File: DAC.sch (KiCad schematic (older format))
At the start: 1 part

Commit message: Add DAC
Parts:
- removed DD?: AD1955, symbol AD1955
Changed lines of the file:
@@
 $Descr A4 11693 8268
 encoding utf-8
-Sheet 1 3
+Sheet 1 1
 Title ""
 Date ""
@@
 Comment4 ""
 $EndDescr
-$Sheet
-S 0    -100 11650 8400
-U 588A0618
-F0 "SatelitesPowerAmplifier" 60
-F1 "SatelitesPowerAmplifier.sch" 60
-$EndSheet
-$Sheet
-S 0    -200 11650 8600
-U 59424E93
-F0 "DAC" 60
-F1 "DAC.sch" 60
-$EndSheet
-$Sheet
-S 0    0    11650 8200
-U 5833169E
-F0 "PowerAmplifier" 60
-F1 "PowerAmplifier.sch" 60
-$EndSheet
-$Comp
-L AD1955 DD?
-U 1 1 5942591C
-P 6700 3350
-F 0 "DD?" H 6700 4297 60  0000 C CNN
-F 1 "AD1955" H 6700 4191 60  0000 C CNN
-F 2 "" H 6700 3600 60  0001 C CNN
-F 3 "" H 6700 3600 60  0001 C CNN
-	1    6700 3350
-	1    0    0    -1
-$EndComp
 $EndSCHEMATC

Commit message: Move DAC circuit from amplifier.sch to DAC.sch
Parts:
- added DD?: AD1955, symbol AD1955
- added DD?: SRC4392I, symbol SRC4392I
- added J?: CONN_01X07, symbol CONN_01X07
- added J?: CONN_01X09, symbol CONN_01X09
- added R?: 3.3k, symbol R
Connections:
- net labels added: GNDA
- wire segments 0 -> 56
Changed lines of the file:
@@
 Comment4 ""
 $EndDescr
+$Comp
+L AD1955 DD?
+U 1 1 5943ADF1
+P 6150 3400
+F 0 "DD?" H 6150 4347 60  0000 C CNN
+F 1 "AD1955" H 6150 4241 60  0000 C CNN
+F 2 "" H 6150 3650 60  0001 C CNN
+F 3 "" H 6150 3650 60  0001 C CNN
+	1    6150 3400
+	1    0    0    -1
+$EndComp
+$Comp
+L SRC4392I DD?
+U 1 1 5943BE8C
+P 3750 2650
+F 0 "DD?" H 3750 4347 60  0000 C CNN
+F 1 "SRC4392I" H 3750 4241 60  0000 C CNN
+F 2 "" H 3800 3350 60  0001 C CNN
+F 3 "" H 3800 3350 60  0001 C CNN
+	1    3750 2650
+	1    0    0    -1
+$EndComp
+Wire Wire Line
+	5500 2900 4400 2900
+Wire Wire Line
+	4400 3000 5300 3000
+Wire Wire Line
+	5300 3000 5300 2700
+Wire Wire Line
+	5300 2700 5500 2700
+Wire Wire Line
+	5500 2800 5200 2800
+Wire Wire Line
+	5200 2800 5200 3100
+Wire Wire Line
+	5200 3100 4400 3100
+Wire Wire Line
+	5500 3700 5400 3700
+Wire Wire Line
+	5400 3700 5400 4250
+Wire Wire Line
+	5400 4250 7200 4250
+Wire Wire Line
+	7200 4250 7200 2300
+Wire Wire Line
+	5500 3600 5300 3600
+Wire Wire Line
+	5300 3600 5300 4350
+Wire Wire Line
+	5300 4350 7300 4350
+Wire Wire Line
+	7300 4350 7300 2400
+Wire Wire Line
+	7200 2300 7700 2300
+Wire Wire Line
+	4400 2000 7700 2000
+Wire Wire Line
+	4400 1900 7700 1900
+Wire Wire Line
+	4400 1800 7700 1800
+Wire Wire Line
+	4400 1700 7700 1700
+Wire Wire Line
+	3100 2600 3000 2600
+Wire Wire Line
+	3000 2600 3000 900
+Wire Wire Line
+	3000 900  7600 900
+Wire Wire Line
+	7600 900  7600 1600
+Wire Wire Line
+	7600 1600 7700 1600
+Wire Wire Line
+	7300 2400 7700 2400
+Wire Wire Line
+	4400 2100 5050 2100
+Wire Wire Line
+	5050 2100 5050 1200
+Wire Wire Line
+	5050 1200 5550 1200
+Wire Wire Line
+	4400 2200 5150 2200
+Wire Wire Line
+	5150 2200 5150 1300
+Wire Wire Line
+	5150 1300 5550 1300
+Wire Wire Line
+	4400 2300 5250 2300
+Wire Wire Line
+	5250 2300 5250 1400
+Wire Wire Line
+	5250 1400 5550 1400
+Wire Wire Line
+	4400 2400 5350 2400
+Wire Wire Line
+	5350 2400 5350 1500
+Wire Wire Line
+	5350 1500 5550 1500
+Wire Wire Line
+	4400 1300 4950 1300
+Wire Wire Line
+	4950 1300 4950 1100
+Wire Wire Line
+	4950 1100 5550 1100
+Wire Wire Line
+	4400 1200 4850 1200
+Wire Wire Line
+	4850 1200 4850 1000
+Wire Wire Line
+	4850 1000 5550 1000
+Wire Wire Line
+	4400 2500 5450 2500
+Wire Wire Line
+	5450 2500 5450 1600
+Wire Wire Line
+	5450 1600 5550 1600
+$Comp
+L CONN_01X07 J?
+U 1 1 5A0C051E
+P 5750 1300
+F 0 "J?" H 5828 1341 50  0000 L CNN
+F 1 "CONN_01X07" H 5828 1250 50  0000 L CNN
+F 2 "" H 5750 1300 50  0001 C CNN
+F 3 "" H 5750 1300 50  0001 C CNN
+	1    5750 1300
+	1    0    0    -1
+$EndComp
+$Comp
+L CONN_01X09 J?
+U 1 1 5A0C063A
+P 7900 2000
+F 0 "J?" H 7978 2041 50  0000 L CNN
+F 1 "CONN_01X09" H 7978 1950 50  0000 L CNN
+F 2 "" H 7900 2000 50  0001 C CNN
+F 3 "" H 7900 2000 50  0001 C CNN
+	1    7900 2000
+	1    0    0    -1
+$EndComp
+$Comp
+L R R?
+U 1 1 5B040832
+P 5200 4500
+F 0 "R?" H 5270 4546 50  0000 L CNN
+F 1 "3.3k" H 5270 4455 50  0000 L CNN
+F 2 "" V 5130 4500 50  0001 C CNN
+F 3 "" H 5200 4500 50  0001 C CNN
+	1    5200 4500
+	1    0    0    -1
+$EndComp
+Wire Wire Line
+	5200 4350 5200 3500
+Wire Wire Line
+	5200 3500 5500 3500
+$Comp
+L GNDA #PWR?
+U 1 1 5B0409AF
+P 5200 4700
+F 0 "#PWR?" H 5200 4450 50  0001 C CNN
+F 1 "GNDA" H 5205 4527 50  0000 C CNN
+F 2 "" H 5200 4700 50  0001 C CNN
+F 3 "" H 5200 4700 50  0001 C CNN
+	1    5200 4700
+	1    0    0    -1
+$EndComp
+Wire Wire Line
+	5200 4700 5200 4650
+Wire Wire Line
+	6800 3400 7100 3400
+Wire Wire Line
+	7100 3400 7100 2200
+Wire Wire Line
+	7100 2200 7700 2200
+Wire Wire Line
+	6800 3300 7000 3300
+Wire Wire Line
+	7000 3300 7000 2100
+Wire Wire Line
+	7000 2100 7700 2100
 $EndSCHEMATC

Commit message: DAC modifications
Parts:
- added J?: I2S 1, symbol CONN_01X05
- added J?: I2S 2, symbol CONN_01X05
- added J?: I2S USB, symbol CONN_01X05
- added J?: I2S HDMI, symbol CONN_01X05
- added J?: Ext DAC, symbol CONN_01X05
- added JP? (x3): DAC ON, symbol Jumper_NC_Small
- added U? (x2): 74HC244, symbol 74HC244
- added U?: ATMEGA88A-PU, DIL28, symbol ATMEGA88A-PU
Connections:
- net labels added: GNDD
- wire segments 56 -> 199
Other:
- moved on the sheet: DD?, R?

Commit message: DAC changes
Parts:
- removed J?: CONN_01X07, symbol CONN_01X07
- removed J?: CONN_01X09, symbol CONN_01X09
- removed J?: I2S 1, symbol CONN_01X05
- removed J?: I2S 2, symbol CONN_01X05
- removed J?: I2S USB, symbol CONN_01X05
- removed J?: I2S HDMI, symbol CONN_01X05
- removed J?: Ext DAC, symbol CONN_01X05
- removed U? (x2): 74HC244, symbol 74HC244
- added C? (x8): 0.1, symbol C_Small
- added DD??: CDCLVC1104, symbol CDCLVC1104
- added J?: To external DAC, symbol CONN_01X04
- added J?: SRC Pins, symbol CONN_01X12
- added J?: DSD Input, symbol CONN_01X04
- added J?: I2S Input, symbol CONN_01X04
- added J?: DAC Pins, symbol CONN_01X05
- added J?: SPDIF Inputs, symbol CONN_01X05
- added J?: CONN_01X05, symbol CONN_01X05
- added R? (x7): 75, symbol R
- added R?: 1k, symbol R
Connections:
- wire segments 199 -> 213
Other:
- moved on the sheet: DD?, JP?, R?, U?

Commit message: Add power
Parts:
- removed R?: 1k, symbol R
- added C? (x2): 2.2, symbol CP_Small
- added C? (x3): 0.1, symbol C_Small
- added C? (x6): 1.0, symbol C_Small
- added C?: 3.3, symbol CP_Small
- added C?: 6.8, symbol CP_Small
- added DA? (x3): LP5900, symbol LP5900
- added J?: MUTE/~RST, symbol CONN_01X03
- added J?: I2S Fs, symbol CONN_01X04
- added R?: 10, symbol R-RESCUE-amplifier
- added R?: 1k, symbol R
- J?: value CONN_01X05 -> Input select
- R? (x8): symbol R -> R-RESCUE-amplifier
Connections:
- net labels added: +1V8, +3.3V, +3V3, +5V, DGND
- wire segments 213 -> 261
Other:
- moved on the sheet: DD??, J?, U?

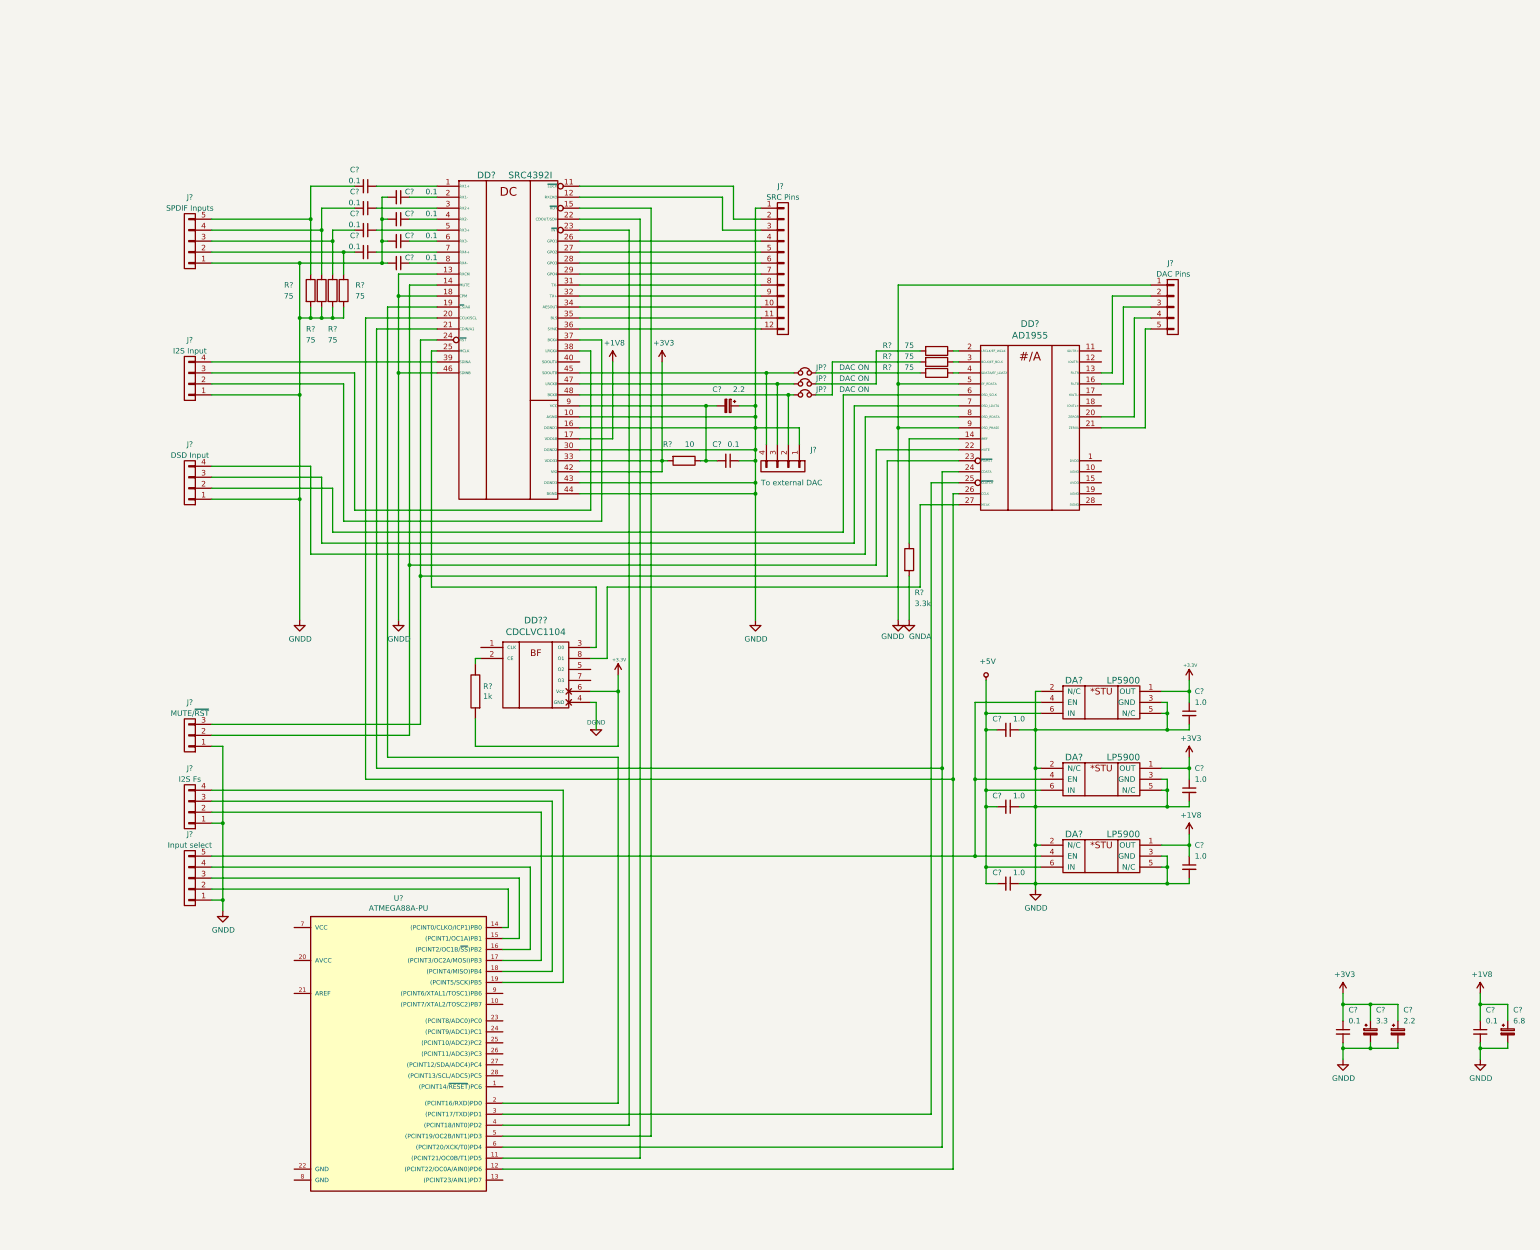
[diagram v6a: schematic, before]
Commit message: Add generators and ad8066
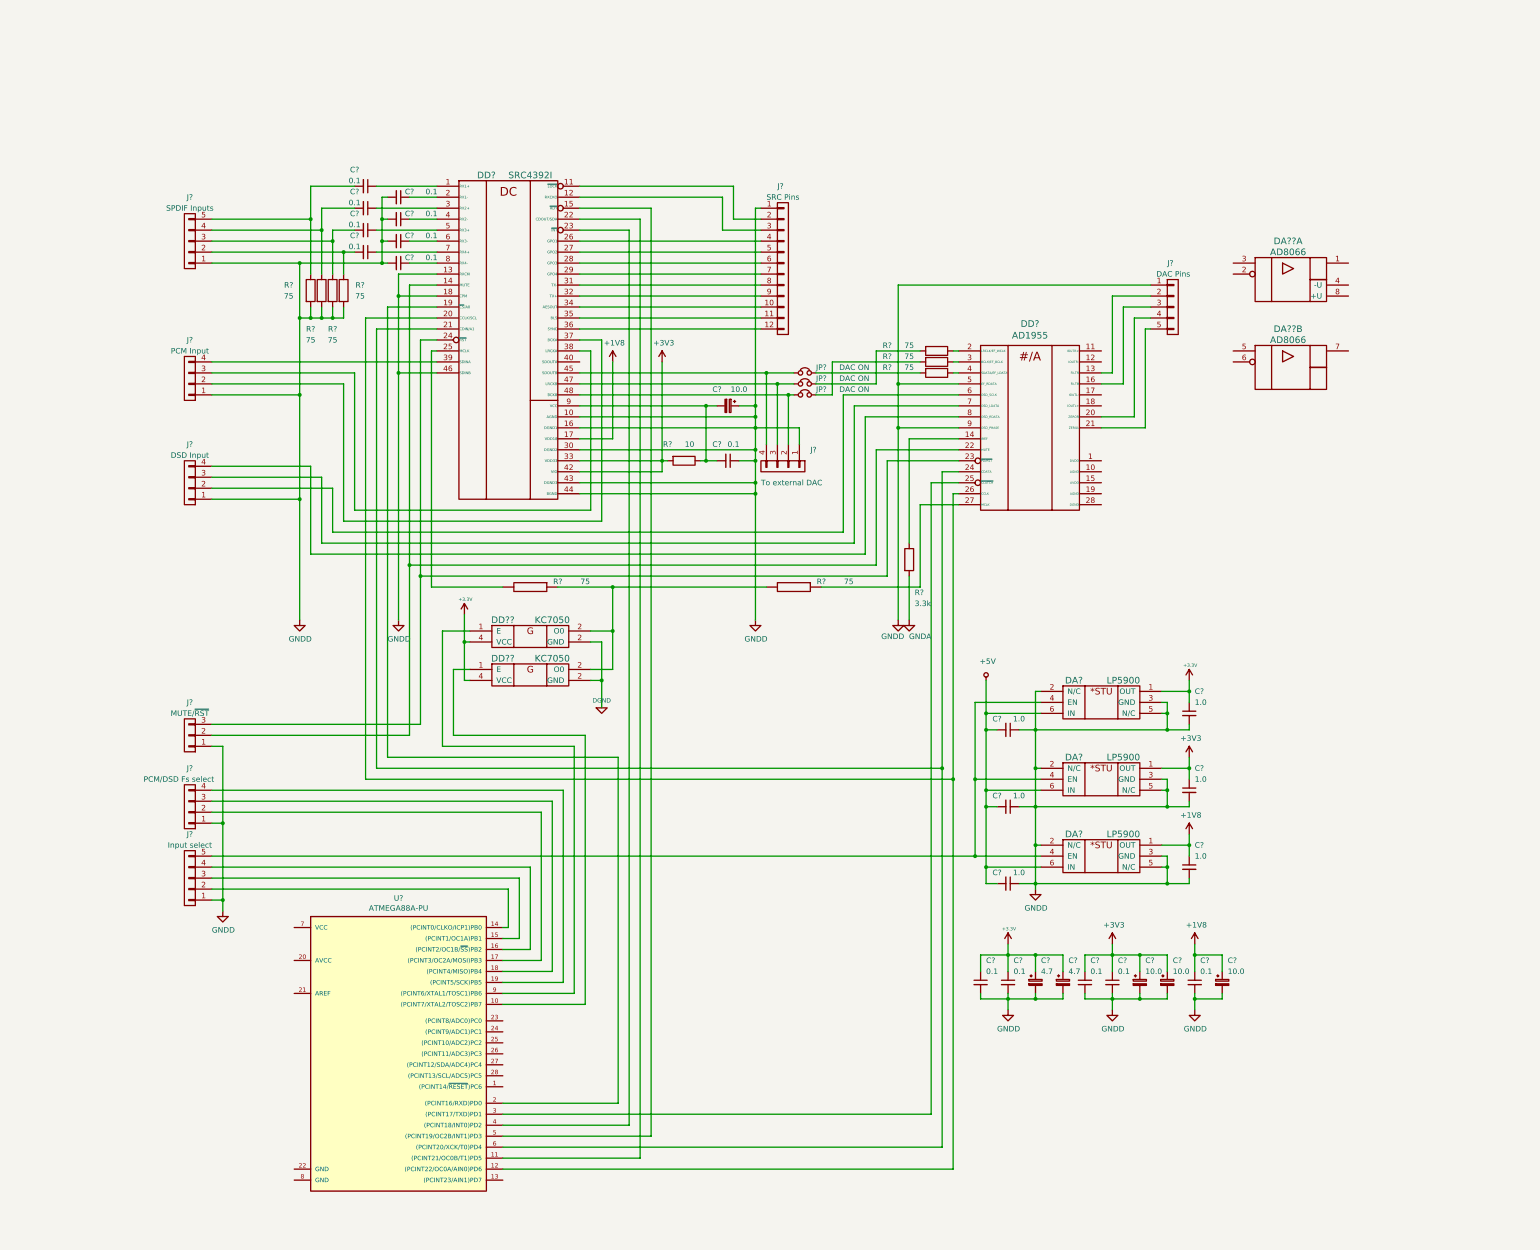
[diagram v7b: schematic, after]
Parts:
- removed DD??: CDCLVC1104, symbol CDCLVC1104
- removed R?: 1k, symbol R
- added C? (x3): 0.1, symbol C_Small
- added C? (x2): 4.7, symbol CP_Small
- added DA?? (x2): AD8066, symbol AD8066
- added DD?? (x2): KC7050, symbol KC7050
- added R? (x2): 75, symbol R
- C? (x2): value 2.2 -> 10.0
- C?: value 3.3 -> 10.0
- C?: value 6.8 -> 10.0
- J?: value I2S Input -> PCM Input
- J?: value I2S Fs -> PCM/DSD Fs select
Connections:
- net +3V3: now also C?.1, C?.1, C?.1, C?.1, C?.1, DD??.4 (VCC), DD??.4 (VCC)
- net DGND: now also DD??.2 (O0), DD??.2 (O0)
- net GNDD: now also C?.2, C?.2, C?.2, C?.2, C?.2
- net at DD?.27 (MCLK): now also R?.1
- net at DD?.25 (MCLK): now also R?.2
- net at U?.10 ((PCINT7/XTAL2/TOSC2)PB7): now also DD??.1 (E)
- net at U?.9 ((PCINT6/XTAL1/TOSC1)PB6): now also DD??.1 (E)
- new net: DD??.2 (O0), DD??.2 (O0), R?.1, R?.2
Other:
- moved on the sheet: C?

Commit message: Add more power for DAC
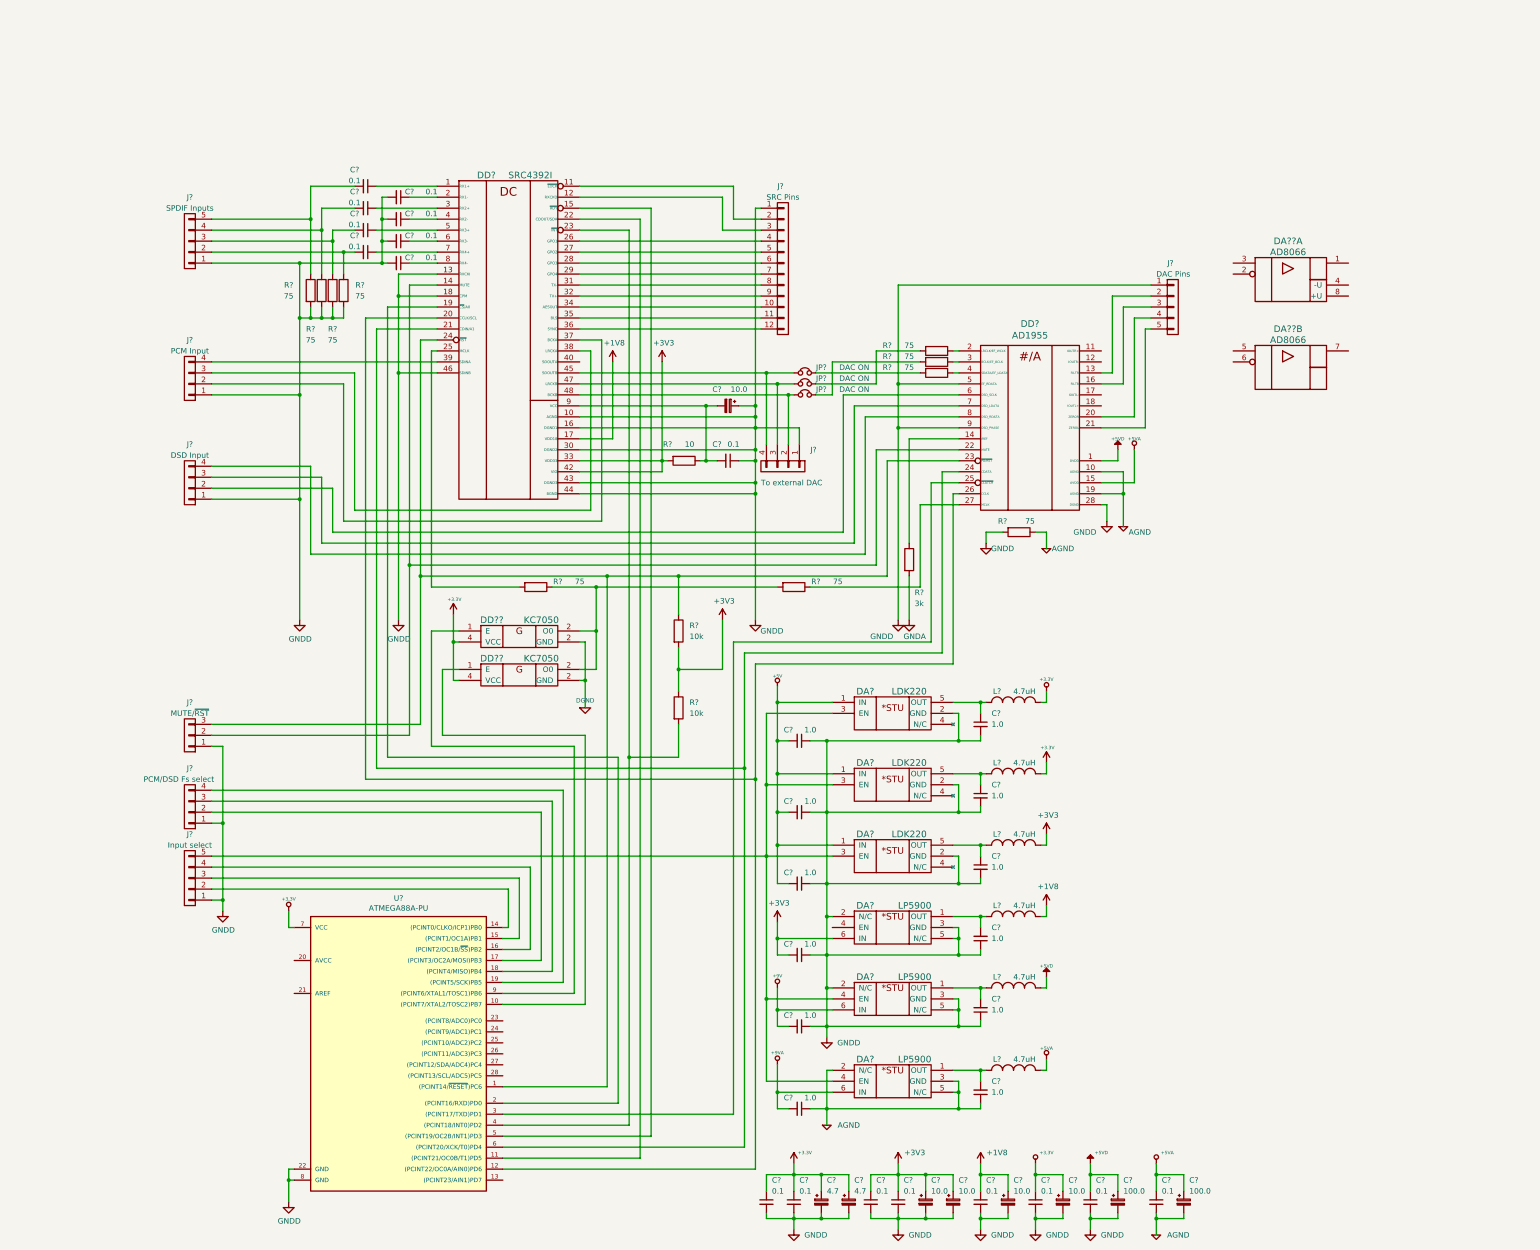
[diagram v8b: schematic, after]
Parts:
- removed R? (x2): 75, symbol R
- added C? (x6): 1.0, symbol C_Small
- added C? (x3): 0.1, symbol C_Small
- added C?: 10.0, symbol CP_Small
- added C? (x2): 100.0, symbol CP_Small
- added DA? (x3): LDK220, symbol LDK220
- added L? (x6): 4.7uH, symbol INDUCTOR_SMALL
- added R? (x3): 75, symbol R-RESCUE-amplifier
- added R? (x2): 10k, symbol R-RESCUE-amplifier
- R?: value 3.3k -> 3k
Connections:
- net +1V8: now also L?.2; no longer C?.1, DA?.1 (OUT)
- net +3V3: now also C?.2, DA?.6 (IN), L?.2, L?.2, R?.1, R?.2; no longer C?.1, C?.1, DA?.1 (OUT), DA?.1 (OUT)
- net +5V: now also C?.2, DA?.1 (IN), DA?.1 (IN), DA?.1 (IN); no longer C?.2, DA?.6 (IN), DA?.6 (IN), DA?.6 (IN)
- net GNDD: now also C?.1, DD?.28 (DGND), U?.22 (GND), U?.8 (GND), C?.1, C?.1, C?.1, C?.2, C?.2, C?.2, C?.2, C?.2, DA?.2 (GND), DA?.2 (GND), DA?.2 (GND), R?.2; no longer C?.2, DA?.2 (N/C), DA?.3 (GND), DA?.5 (N/C)
- net +5VD: now reaches DD?.1 (DVDD)
- net +5VD: now also C?.1, C?.1, L?.2
- net AGND: now reaches DD?.10 (AGND)
- net AGND: now also DA?.2 (N/C), DA?.3 (GND), DA?.5 (N/C), DD?.19 (AGND), C?.1, C?.1, C?.2, C?.2, R?.1
- net +5VA: now reaches DD?.15 (AVDD)
- net +5VA: now also C?.1, C?.1, L?.2
- net at DD?.23 (~PD/RST), DD?.24 (~RST), J?.3 (P3): now also U?.1 ((PCINT14/~RESET~)PC6), R?.1
- net at DD?.27 (MCLK): now also R?.1
- net at DD?.23 (~INT), U?.4 ((PCINT18/INT0)PD2): now also R?.2
- net at DD?.25 (MCLK): now also R?.2
- net +3.3V: now reaches U?.7 (VCC)
- net +3.3V: now also C?.1, C?.1, L?.2
- net at DA?.4 (EN), DA?.4 (EN), J?.5 (P5): now also DA?.3 (EN), DA?.3 (EN), DA?.3 (EN); no longer DA?.4 (EN)
- new net: C?.2, DA?.1 (OUT), L?.1 (x3)
- new net: C?.1, DA?.5 (OUT), L?.1 (x3)
- new net: DD??.2 (O0), DD??.2 (O0), R?.1, R?.2
- new net +9V: C?.2, C?.2, DA?.6 (IN), DA?.6 (IN)
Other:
- moved on the sheet: C?, DA?, DD??
